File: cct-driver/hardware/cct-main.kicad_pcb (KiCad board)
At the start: 2 copper layers, 130 x 164 mm, 217 parts, among them J1 C707824, J10 C37815, J11 C474923, J2 C165948, J3 C441333, J4 C441333, J5 C441333, J6 C441333, J7 C441333, J8 C441333, J9 C2906270, Q1 C3281500, Q10 C2890395, Q11 C2890395, Q12 C2890395, Q13 C2890395, Q14 C2890395, Q15 C2890395, Q16 C2890395, Q17 C2890395, Q18 C2890395, Q2 C3281500, Q3 C20526, Q4 C2146, Q5 C2146, Q6 C20526, Q7 C2890395, Q8 C2890395, Q9 C2890395, SW1 C318884, SW2 C318884, U1 C2864837, U2 C524806, U3 C6186, U4 C701341, U5 C84681, U6 C52140501, U7 C52140501

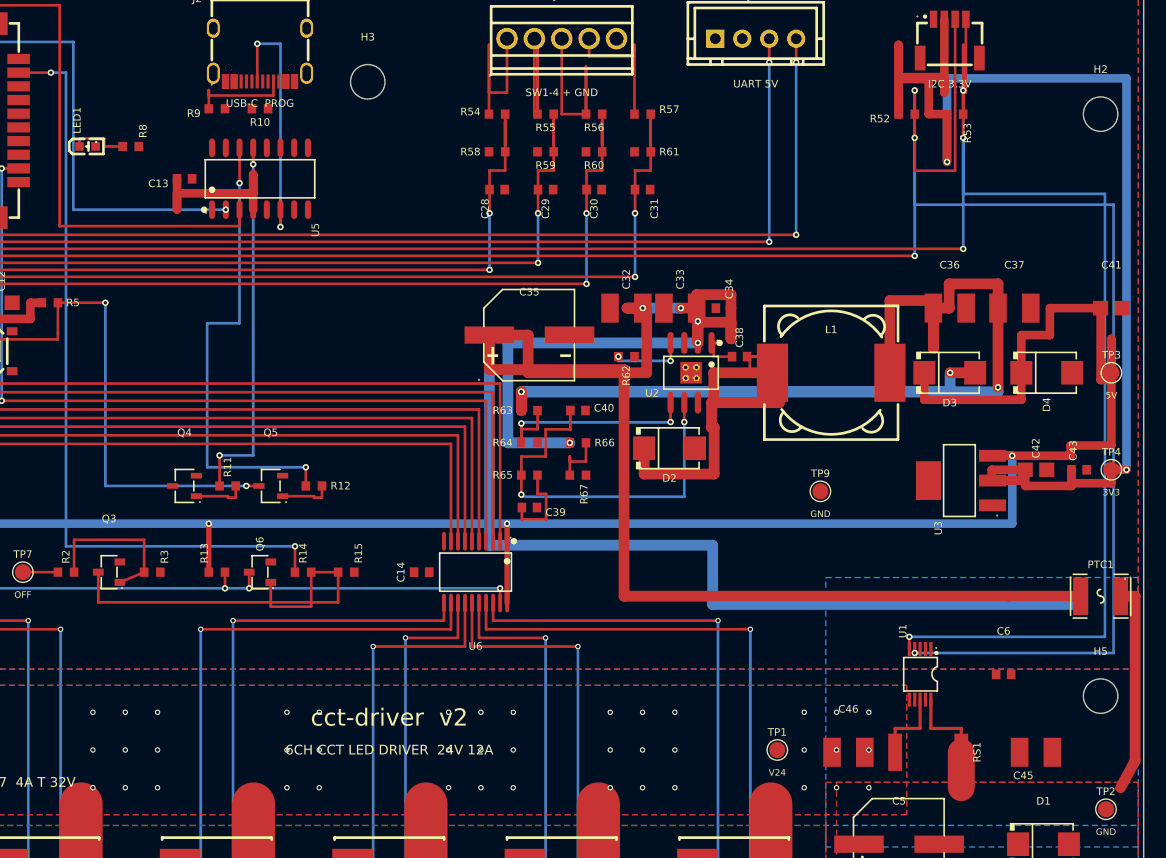
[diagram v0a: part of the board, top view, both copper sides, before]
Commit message: v2:DFM 两个老脚本复跑 + 五处 DRC 收干净(交叉 3→1,间距 12→8,其余归零)
`gen_dfm_fixes.py`(U2 散热焊盘下的 4 个热过孔、EP 锡膏收缩、J2 两个定位孔改 NPTH)
与 `gen_mask_dam.py`(J2 的阻焊桥加宽)都在新板上复跑通过 —— 它们本来就是幂等的,
只是之前一直没跑。**这两个要排在布线之后**,否则会被重铺覆铜盖掉。

顺手把五类 DRC 逐条查清根因收掉:
- **两条底层线交叉,是因为它们都得穿过 V5_SYS 那条底层横轨** —— 给 V24_LOGIC
  在 x=92 上一小段顶层跳过去;OE_CTRL 那条改成让横轨先铺、它再避
- 覆铜「优先级必须互异」:GND 那块汇合颈与另外两块同为 5,改成 6
- I2C 下到 U1 的两个换层孔离 U1 的脚只剩 0.20mm(要 0.25),拐点各下移 1.6mm
- V24_PROT 沿右板边那一段离板边只剩 0.30mm(要 0.50),从 x=129.2 收到 128.8

    走线 780 段 · 过孔 256 颗 · 覆铜 16 块
    短路 0 · 走线交叉 1 · 间距 8(全是 J2/U2 封装自带的,老板子上也有)
    未连接 49 条
    覆铜优先级 / 孔间距 / 板边间距 / 共位孔 全部归零

完整流水线(顺序不能乱):
    gen_pcb_v2 → gen_silk_v2 → gen_silk_refdes_fix → gen_route_v2 → gen_dfm_fixes → gen_mask_dam

Co-Authored-By: Claude <noreply@anthropic.com>
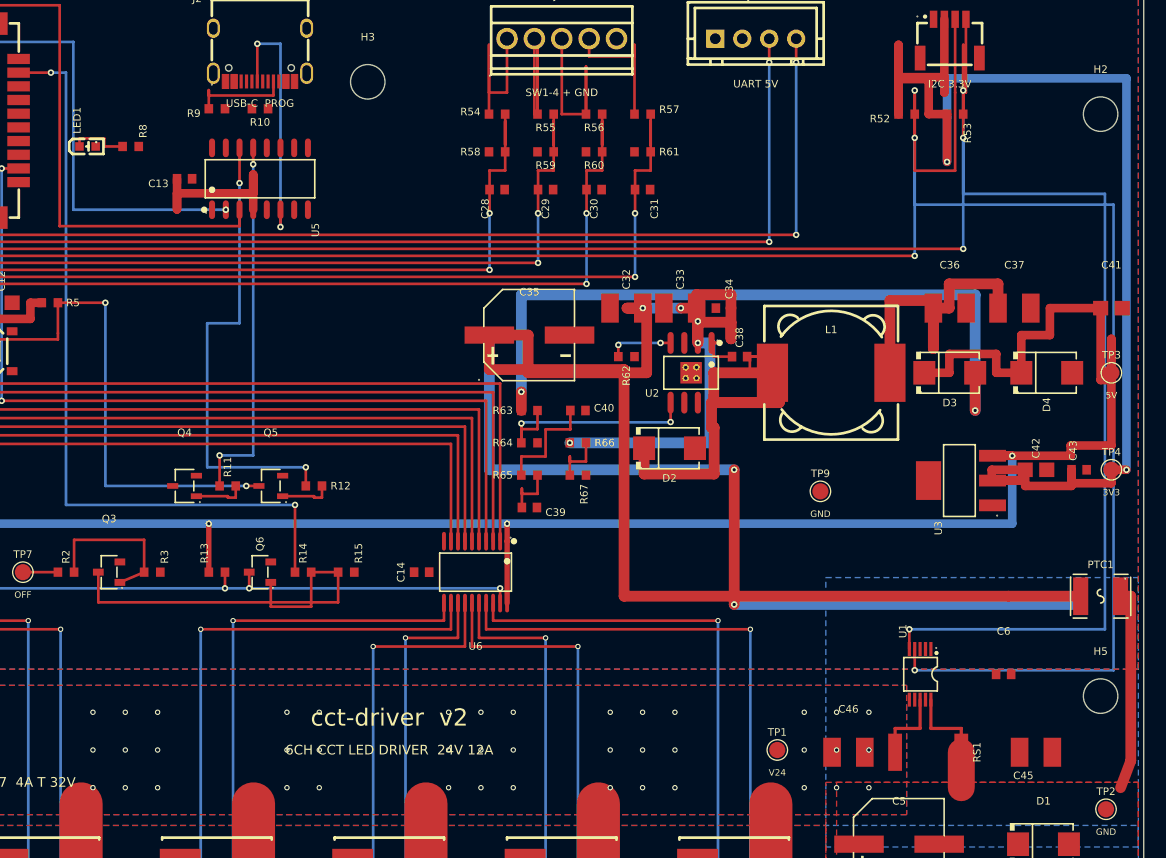
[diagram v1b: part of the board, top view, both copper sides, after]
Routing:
- net V5_BUCK: track 128.8 -> 96.5 mm, vias 4 -> 2
- net COMP: track 36.4 -> 10.5 mm, vias 2 -> 0
- net V24_LOGIC: track 244.8 -> 235.6 mm, vias 5 -> 7
- net I2C_SDA: track 227.1 -> 230.3 mm
- net COMP_Z: track 8.25 -> 5.41 mm
- net V5_SYS: track 183.0 -> 181.5 mm
- net RT_CLK: track 6.92 -> 6.12 mm
- net V24_PROT: track 33.4 -> 32.8 mm

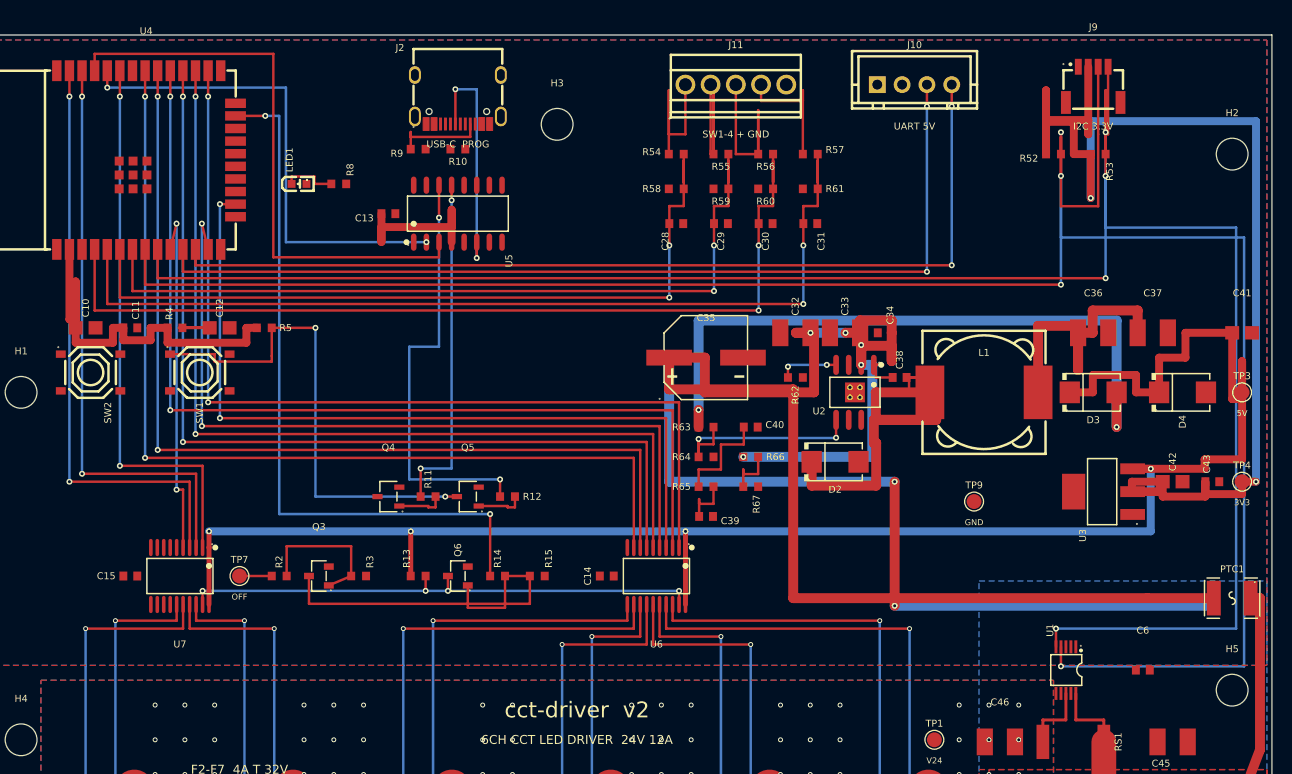
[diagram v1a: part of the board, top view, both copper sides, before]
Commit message: v2 布线:走廊自己扫、短线按难度排队;未连接 49 → 47,短路 0
两条**让它不再一碰就碎**的改动:

1. **`corridor()` 的走廊位置改成自己扫,调用方给的值只当「先试这几个」。**
   原来要求调用方给一串候选 y/x —— 而那些数是跟着某一版摆位手调出来的,
   摆位一动(哪怕只挪 0.5mm)十几条干线一起失效,还看不出为什么。
   现在给的值只排优先,后面接一遍从 a 到 b 之间外扩 8mm、步长 0.5mm 的密扫,横竖都扫。
2. **短连线改成先收齐、再按「跑得远的先挑路」统一跑。** 顺手就布的话,
   近的会先把窄缝占掉,远的反而绕不出去 —— 同一批线换个顺序,通与不通差 4 条。

另外两处摆位按实测挪开:
- **A4 那七颗分压件原来叠在同一个 x 上** —— 每颗的两只脚上下都是另一颗的脚,
  从中间任何一只脚都出不去线。改成两列。
- 改完之后它们又正好压在 **12 路 PWM 最后扎进 U6 输入脚的那一束竖线**(x 64–72)上,
  再整体右移到 x 75/79。这一步是渲染 DRC 报出三条短路才发现的,**不是猜的**。

    走线 783 段 · 过孔 256 颗 · 覆铜 16 块
    **短路 0** · 走线交叉 1 · 间距 6(J2/U2 封装自带)
    未连接 47 条
    网表与原理图 525 条零差异

Co-Authored-By: Claude <noreply@anthropic.com>
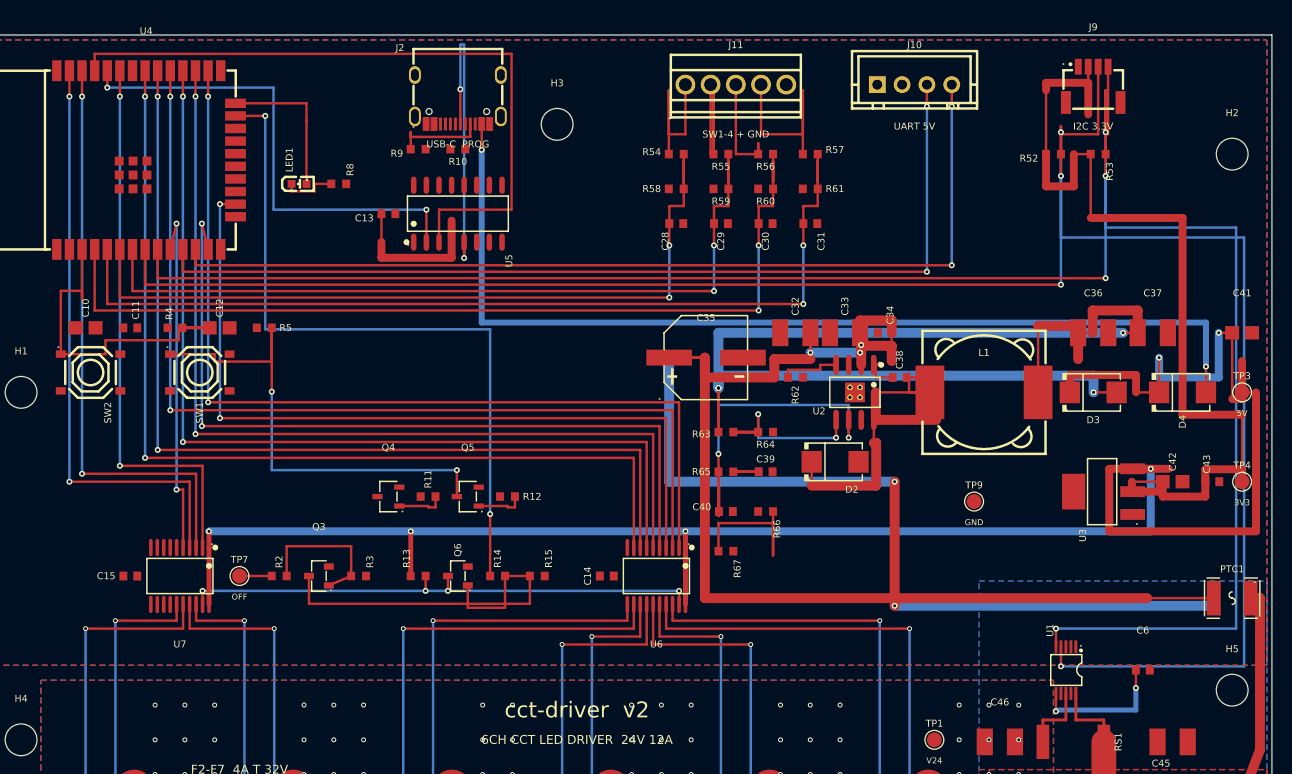
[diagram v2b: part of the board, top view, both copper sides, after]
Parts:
- moved C40 8.86 mm to (75.0, 48.0)
- moved C39 7.50 mm to (79.0, 44.0)
- moved R67 6.96 mm to (75.0, 52.0)
- moved R64 6.50 mm to (79.0, 40.0)
- moved R66 5.70 mm to (79.0, 48.0)
- moved R65 2.50 mm to (75.0, 44.0)
- moved R63 2.06 mm to (75.0, 40.0)
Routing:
- net USB_VBUS: track 0.00 -> 100.0 mm, vias 0 -> 2
- net V3P3: track 181.6 -> 132.9 mm
- net RTS: track 43.5 -> 0.00 mm, vias 2 -> 0
- net DTR: track 34.5 -> 0.00 mm, vias 2 -> 0
- net EN: track 9.07 -> 41.2 mm
- net USB_DP: track 0.00 -> 31.5 mm, vias 0 -> 2
- net V5_SYS: track 181.5 -> 212.9 mm, vias 4 -> 6
- net V5_BUCK: track 96.5 -> 126.9 mm, vias 2 -> 4
- net COMP: track 10.5 -> 38.8 mm, vias 0 -> 2
- net V24_LOGIC: track 235.6 -> 209.5 mm, vias 7 -> 5
- net USB_DM: track 24.2 -> 0.00 mm, vias 2 -> 0
- net LED_STATUS: track 0.00 -> 15.3 mm
- net I2C_SDA: track 230.3 -> 218.0 mm
- net U0TXD: track 58.4 -> 70.0 mm
- net EN_BUCK: track 5.43 -> 16.0 mm
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
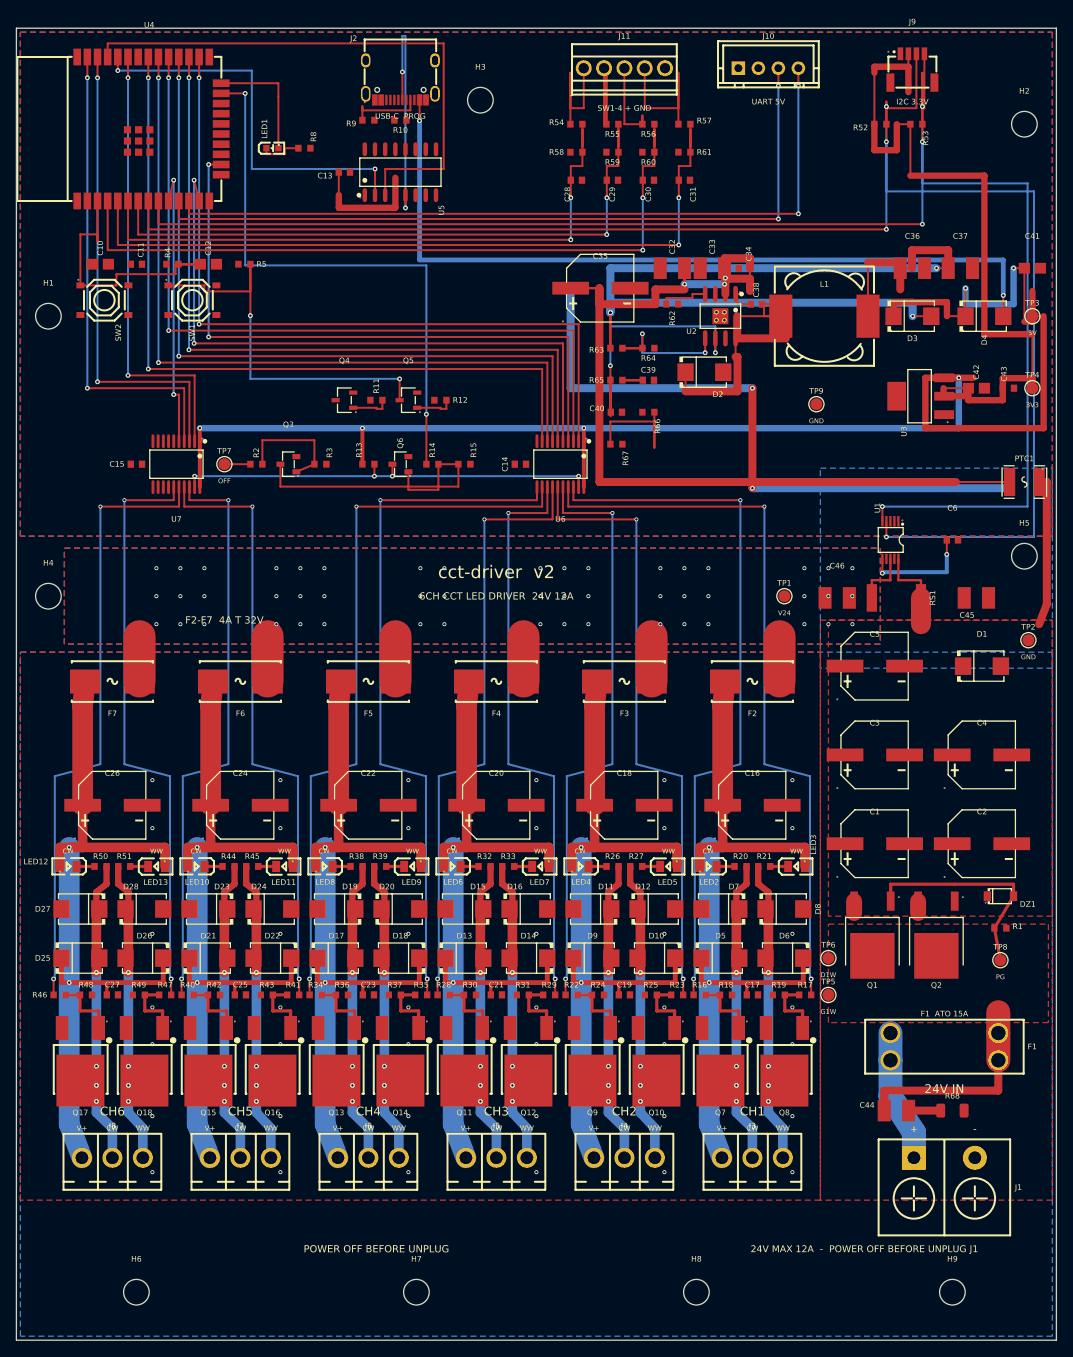
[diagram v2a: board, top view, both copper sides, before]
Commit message: v2:悬空铜清干净(悬空过孔 6→1、悬空走线 2→0)
两处都是**实打实的接不上**,不是警告级的挑剔:

- **PTC1 和 C35 是贴片件,焊盘只在顶层。** 我从它们的脚上直接起了一条底层线 ——
  那条线两头其实都悬着,板子上根本没接通。改成走顶层出脚、中途再换层。
- **每列那几颗 GND 缝合过孔里,有两个 y 挑错了**:122.4 压在栅极下游那根线上、
  127 落在 MOS 的散热片焊盘里。只留确实空着的五条横带。

顺手对着渲染图又看了一遍:丝印全部落在板框内、`F2-F7 4A T 32V` 从保险丝座底下
(被座体挡住)挪进脊椎带、`24V IN` 从 R68 的位号上挪开、端子那两行落在
MOS 下沿与端子体上沿之间那 3.36mm 里 —— 现在插座装上去也挡不住。

    走线 776 段 · 过孔 246 颗 · 覆铜 16 块
    短路 0 · 悬空走线 0 · 悬空过孔 1
    未连接 49 条(卡在 `hardware/PENDING-DECISION.md` 那个待拍板的取舍上)
    网表与原理图 525 条零差异

Co-Authored-By: Claude <noreply@anthropic.com>
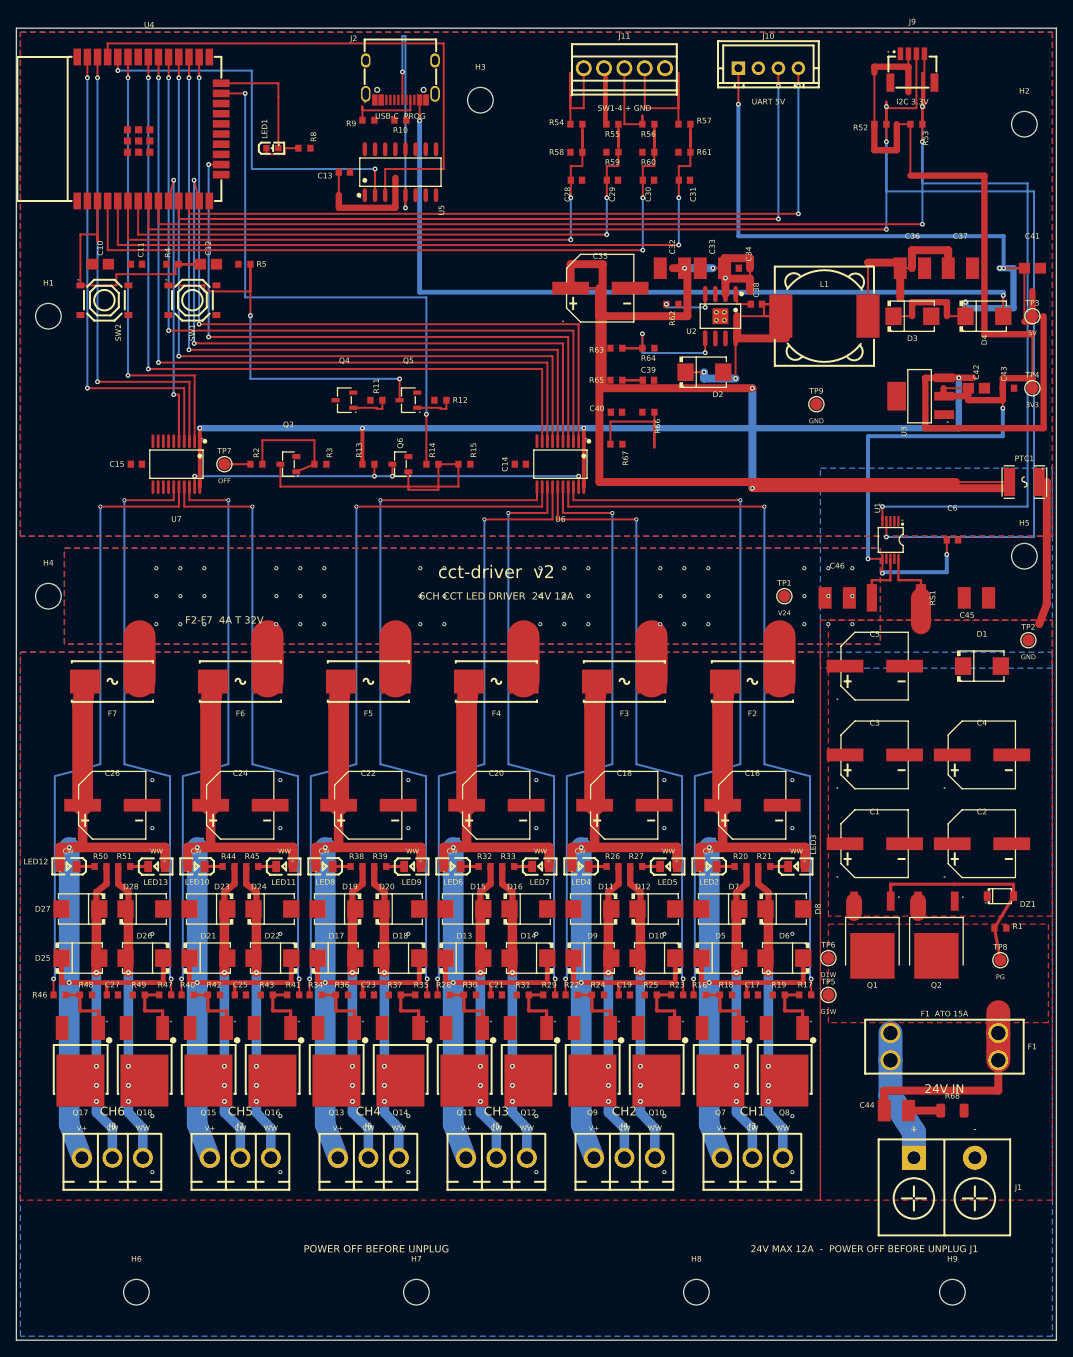
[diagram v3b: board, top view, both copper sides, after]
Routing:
- net V5_BUCK: track 126.9 -> 29.4 mm, vias 4 -> 0
- net V5_SYS: track 212.9 -> 274.6 mm, vias 6 -> 8
- net V3P3: track 132.9 -> 172.9 mm, vias 2 -> 4
- net COMP: track 38.8 -> 0.00 mm, vias 2 -> 0
- net V24_LOGIC: track 209.5 -> 218.2 mm
- net SW_NODE: track 45.3 -> 41.6 mm, vias 0 -> 2
- net RT_CLK: track 6.12 -> 6.92 mm, vias 0 -> 2
- net GND: vias 37 -> 31
- net CH6_WW_GR: vias 1 -> 0
- net CH5_WW_GR: vias 1 -> 0
- net CH4_WW_GR: vias 1 -> 0
- net CH3_WW_GR: vias 1 -> 0
- net CH2_WW_GR: vias 1 -> 0
- net CH1_WW_GR: vias 1 -> 0

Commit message: v2 布线:写了个真正的迷宫布线(A*,两层),未连接 47 → 29,短路仍是 0
**为什么最后还是得写它。** 前面那套「候选拐法」(L / Z / 五点 / 逃逸点组合)本质上是在
**猜路径的形状** —— 板子一挤就猜不中,而且每次摆位一动,猜中的那几条又全变。
A* 不猜:把已有的铜按 0.25mm 栅格化成两层障碍图,从起点搜到终点,搜不到就是真的没路。

它**仍然不是自动布线器**:一次只走一条线、不拆别人的线、不迭代重布、走不通照样记账报出来。
换层按 14 的代价计、拐弯按 2 计,所以出来的路是「能直就直、少打孔」的。

四个只有实跑才会发现的坑,都写进注释了:
- **换层的那个格子要按过孔(⌀0.6)另查一遍**,拿走线的余量去判,过孔会贴到隔壁焊盘上
- **不许连着两步换层**,否则打出两个只隔 0.25mm 的孔
- **起点终点必须落在顶层** —— 焊盘几乎都是顶层贴片,路径在底层收尾就接不到焊盘(悬空)
- **同网络 0.7mm 内已有孔就不再打**;换层也躲开已有孔 0.8mm

另外三件:
- **地平面缝合挪到所有布线之后**(76 颗)。早先放在布线之前,后面那些成束规划的线
  是按规划直接落笔、不查已有铜的,结果一堆缝合孔被压上 —— DRC 报 10 处短路。
- **天线禁区从 x0–8 收到 x0–7.0**:U4 那两颗角上的 GND 焊盘从 x=7.125 起,
  禁到 8.0 会把它们圈在里面,地覆铜够不着,板上是真的接不上。
- 靠覆铜连、但覆铜够不着的那些电源支线(V3P3 / V5_SYS 等),按最近邻串成链逐段交给迷宫。

    走线 1082 段 · 过孔 372 颗 · 覆铜 16 块
    **短路 0 · 悬空过孔 0 · 钻孔间距 0 · 走线交叉 1**
    间距 6(全是 J2/U2 封装自带的,老板子上也有)
    未连接 29 条(今天开工时是 133)
    网表与原理图 525 条零差异

Co-Authored-By: Claude <noreply@anthropic.com>
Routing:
- net V3P3: track 172.9 -> 431.5 mm, vias 4 -> 26
- net V5_BUCK: track 29.4 -> 213.4 mm, vias 0 -> 7
- net V24_BUS: track 41.2 -> 175.9 mm
- net V5_SYS: track 274.6 -> 391.5 mm, vias 8 -> 6
- net V24_PROT: track 32.8 -> 140.7 mm, vias 0 -> 4
- net CH1_WW_D: track 38.8 -> 111.2 mm
- net COMP: track 0.00 -> 66.1 mm, vias 0 -> 4
- net IO0: track 50.0 -> 89.3 mm, vias 2 -> 4
- net RTS: track 0.00 -> 37.9 mm, vias 0 -> 4
- net PMOS_GATE: track 27.7 -> 63.5 mm
- net DTR: track 0.00 -> 34.7 mm, vias 0 -> 4
- net EN_BUCK: track 16.0 -> 48.3 mm, vias 0 -> 2
- net V24_LOGIC: track 218.2 -> 246.4 mm
- net FB_5V: track 22.6 -> 43.9 mm, vias 2 -> 4
- net CH1_WW_GR: track 8.16 -> 24.2 mm
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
